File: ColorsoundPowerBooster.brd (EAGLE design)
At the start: 78.4 x 45.7 mm, 58 parts, among them IC1 MAX1044, Q1 BC169, Q2 BC184, Q3 BC109

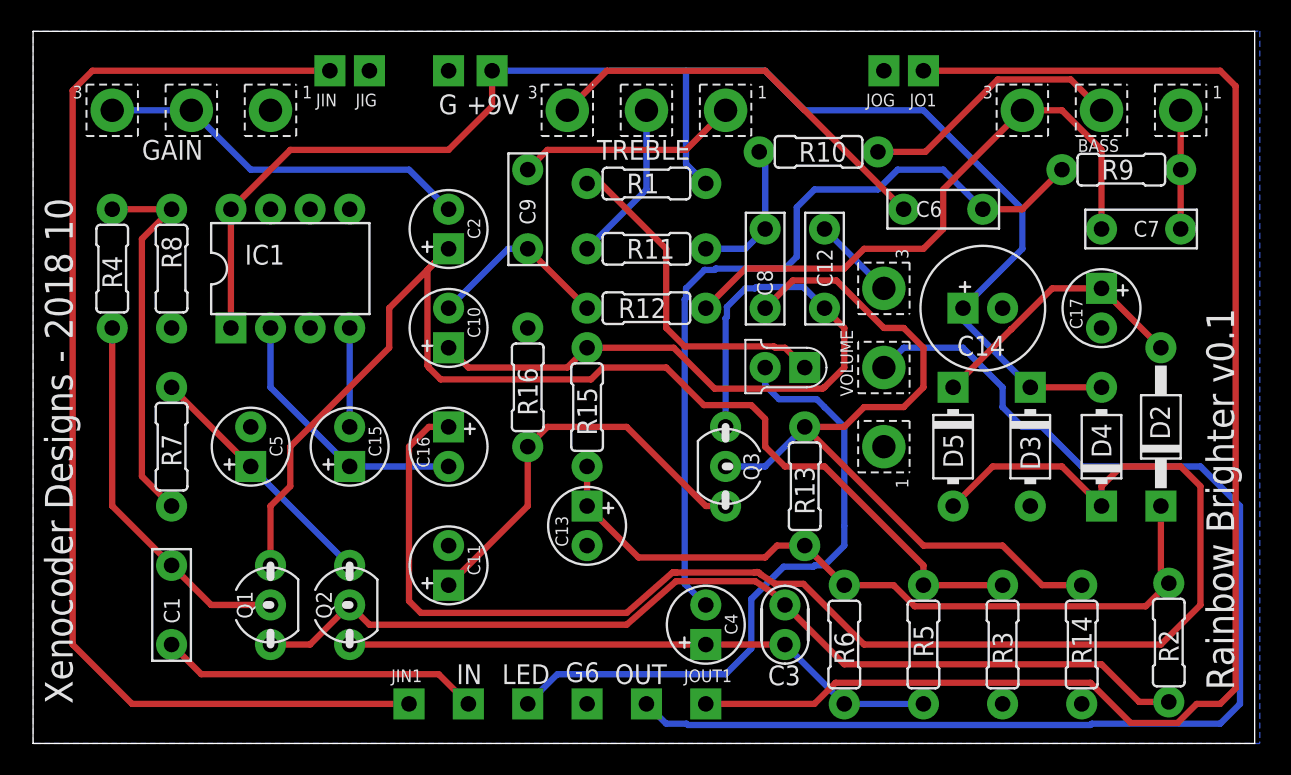
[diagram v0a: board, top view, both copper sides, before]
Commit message: Updated to Version 1.1 to fix Gain and Bass pot wire inversion
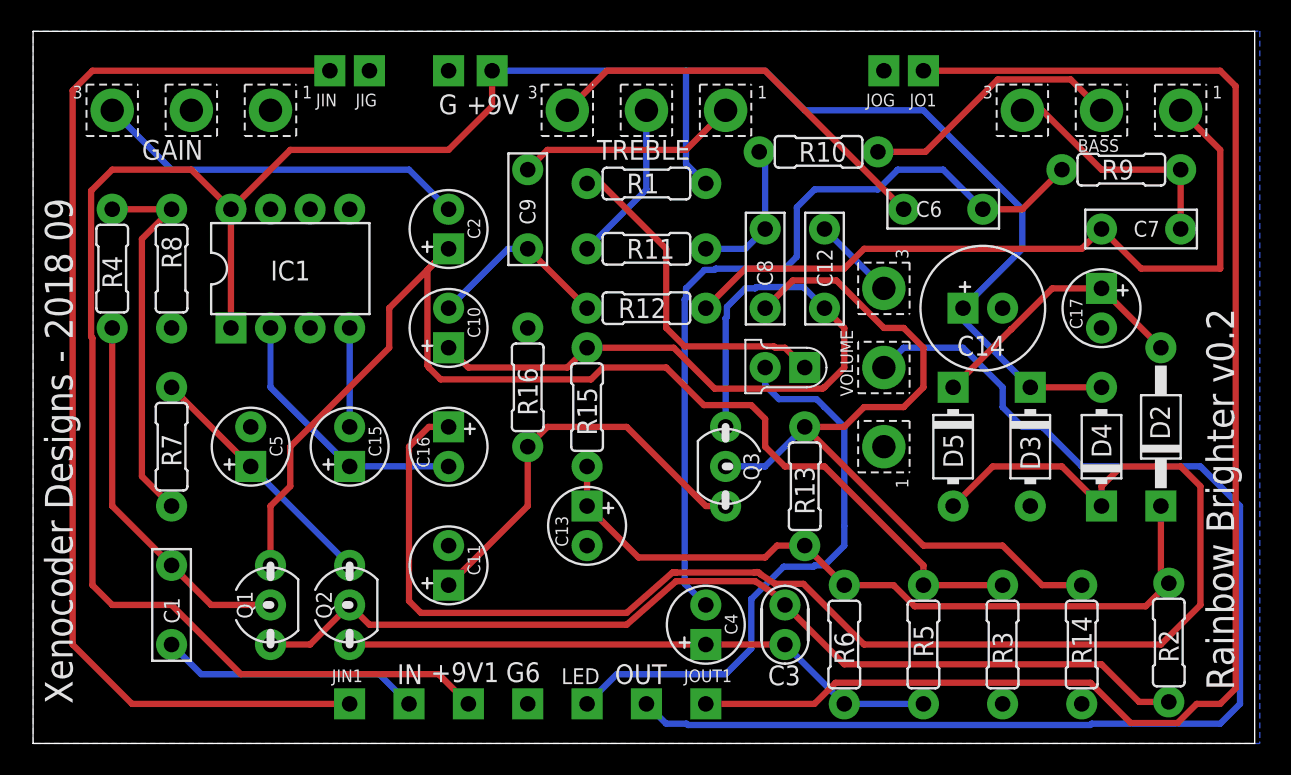
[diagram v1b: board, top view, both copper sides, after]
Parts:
- added +9V1: +9V(T), mb_supply:SQUARE
- moved G6 3.81 mm to (31.8, 2.54)
- moved IN 3.81 mm to (24.1, 2.54)
- moved LED 3.81 mm to (35.6, 2.54)
- moved JIN1 3.81 mm to (20.3, 2.54)
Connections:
- removed net N$14: BASS.1, C7.1, R9.2
- removed net N$15: BASS.3, C7.2, R12.1
- new net N$30: BASS.3, C7.1, R9.2
- new net N$31: BASS.1, C7.2, R12.1
- net +9V: now also +9V1.1
- net GND: now also GAIN.2
- net N$5: no longer GAIN.2
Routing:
- net +9V: track 94.3 -> 157.5 mm
- net N$31: track 0.00 -> 47.4 mm
- net N$15: track 38.3 -> 0.00 mm
- net N$30: track 0.00 -> 15.5 mm
- net N$14: track 7.62 -> 0.00 mm
- net N$22: track 41.3 -> 37.5 mm
- net N$24: track 75.8 -> 72.0 mm
- net IN: track 20.6 -> 16.8 mm
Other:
- board text added: "Rainbow Brighter v0.2"
- board text added: "Xenocoder Designs - 2018 09"
- board text removed: "Rainbow Brighter v0.1"
- board text removed: "Xenocoder Designs - 2018 10"
